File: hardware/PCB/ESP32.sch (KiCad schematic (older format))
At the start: 35 parts, among them IC5 ESP32-D0WD-V3, Q2 SS8050-G, Q3 SS8050-G, U3 ESP32_Antenna, Y1 ABS05-32.768KHZ-T, Y2 ABM11AIG-40.000MHZ-4-1Z-T

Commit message: Use added ABS05 symbol and footprint form project library
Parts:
- removed Y1: ABS05-32.768KHZ-T, ProjectFootprints:ABS05, symbol ABS05-32.768KHZ-T:ABS05-32.768KHZ-T
- added Y?: ABS05-32.768KHZ-T, ABS05, symbol ProjectLibrary:ABS05-32.768KHZ-T
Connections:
- net 32K_XN: now also Y?.2
- net 32K_XP: now also Y?.1
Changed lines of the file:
@@
 	6100 5900 6600 5900
-$Comp
-L ABS05-32.768KHZ-T:ABS05-32.768KHZ-T Y1
-U 1 1 5FE918FF
-P 1300 6750
-F 0 "Y1" H 1800 6900 50  0000 L CNN
-F 1 "ABS05-32.768KHZ-T" H 1700 6450 50  0000 C CNN
-F 2 "ProjectFootprints:ABS05" H 1950 6850 50  0001 L CNN
-F 3 "" H 1950 6750 50  0001 L CNN
-F 4 "ABRACON - ABS05-32.768KHZ-T - CRYSTAL, 32.768KHZ, 12.5PF, 1.6 X 1MM" H 1950 6650 50  0001 L CNN "Description"
-F 5 "" H 1950 6550 50  0001 L CNN "Height"
-F 6 "815-ABS05-32.768K-T" H 1950 6450 50  0001 L CNN "Mouser Part Number"
-F 7 "https://www.mouser.co.uk/ProductDetail/ABRACON/ABS05-32768KHZ-T/?qs=Pyu0ZBy%2FIJZ5hxIXB%2FLU5A%3D%3D" H 1950 6350 50  0001 L CNN "Mouser Price/Stock"
-F 8 "ABRACON" H 1950 6250 50  0001 L CNN "Manufacturer_Name"
-F 9 "ABS05-32.768KHZ-T" H 1950 6150 50  0001 L CNN "Manufacturer_Part_Number"
-	1    1300 6750
-	-1   0    0    -1
-$EndComp
 $Comp
 L Device:C C?
@@
 Wire Wire Line
 	10650 2350 10650 2500
+$Comp
+L ProjectLibrary:ABS05-32.768KHZ-T Y?
+U 1 1 5FEB4B97
+P 1300 6750
+F 0 "Y?" H 1650 7000 50  0000 L CNN
+F 1 "ABS05-32.768KHZ-T" H 1100 6900 50  0000 L CNN
+F 2 "ABS05" H 1950 6850 50  0001 L CNN
+F 3 "" H 1950 6750 50  0001 L CNN
+F 4 "ABRACON - ABS05-32.768KHZ-T - CRYSTAL, 32.768KHZ, 12.5PF, 1.6 X 1MM" H 1950 6650 50  0001 L CNN "Description"
+F 5 "815-ABS05-32.768K-T" H 1950 6450 50  0001 L CNN "Mouser Part Number"
+F 6 "https://www.mouser.co.uk/ProductDetail/ABRACON/ABS05-32768KHZ-T/?qs=Pyu0ZBy%2FIJZ5hxIXB%2FLU5A%3D%3D" H 1950 6350 50  0001 L CNN "Mouser Price/Stock"
+F 7 "ABRACON" H 1950 6250 50  0001 L CNN "Manufacturer_Name"
+F 8 "ABS05-32.768KHZ-T" H 1950 6150 50  0001 L CNN "Manufacturer_Part_Number"
+	1    1300 6750
+	-1   0    0    -1
+$EndComp
 $EndSCHEMATC

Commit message: Connect ESP32 pins
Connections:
- net SEN_RST: now reaches IC5.34 (GPIO5)
- net I2C_SCL: now reaches IC5.36 (GPIO23)
- net I2C_SDA: now reaches IC5.39 (GPIO22)
- net UART_RX: now reaches IC5.40 (U0RXD)
- net UART_TX: now reaches IC5.41 (U0TXD)
- net BAT_PWR: now reaches IC5.42 (GPIO21)
- net ESP_UART_DTR renamed UART_DTR
- net ESP_UART_RTS renamed UART_RTS
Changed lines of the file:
@@
 $EndComp
 Text HLabel 8350 2150 0    50   Input ~ 0
-ESP_UART_RTS
+UART_RTS
 Text HLabel 8350 1050 0    50   Input ~ 0
-ESP_UART_DTR
+UART_DTR
 Wire Wire Line
 	9150 1050 9250 1050
@@
 	-1   0    0    -1
 $EndComp
+Text HLabel 6600 1800 1    50   Input ~ 0
+UART_RX
+Text HLabel 6500 1800 1    50   Input ~ 0
+UART_TX
+Wire Wire Line
+	6500 1800 6500 1950
+Wire Wire Line
+	6600 1800 6600 1950
+Text HLabel 6400 1800 1    50   Input ~ 0
+BAT_PWR
+Wire Wire Line
+	6400 1950 6400 1800
+Text HLabel 7250 2850 2    50   Input ~ 0
+I2C_SCL
+Wire Wire Line
+	7250 2850 7100 2850
+Text HLabel 6700 1800 1    50   Input ~ 0
+I2C_SDA
+Wire Wire Line
+	6700 1800 6700 1950
+Text HLabel 7250 3050 2    50   Input ~ 0
+SEN_RST
+Wire Wire Line
+	7250 3050 7100 3050
 $EndSCHEMATC

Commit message: Connect Display
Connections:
- net DISP_BS: now reaches IC5.14 (GPIO25)
- net DISP_RES: now reaches IC5.15 (GPIO26)
- net DISP_SDI: now reaches IC5.17 (MTMS)
- net DISP_DC: now reaches IC5.18 (MTDI)
- net DISP_CLK: now reaches IC5.20 (MTCK)
- net DISP_CS: now reaches IC5.21 (MTDO)
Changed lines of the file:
@@
 Wire Wire Line
 	7250 3050 7100 3050
+Text HLabel 6200 5000 3    50   Input ~ 0
+DISP_CLK
+Text HLabel 6300 5000 3    50   Input ~ 0
+DISP_CS
+Text HLabel 5900 5000 3    50   Input ~ 0
+DISP_SDI
+Text HLabel 6000 5000 3    50   Input ~ 0
+DISP_DC
+Text HLabel 5150 3950 0    50   Input ~ 0
+DISP_BS
+Text HLabel 5700 5000 3    50   Input ~ 0
+DISP_RES
+Wire Wire Line
+	5300 3950 5150 3950
+Wire Wire Line
+	5700 5000 5700 4850
+Wire Wire Line
+	5900 5000 5900 4850
+Wire Wire Line
+	6000 5000 6000 4850
+Wire Wire Line
+	6200 5000 6200 4850
+Wire Wire Line
+	6300 5000 6300 4850
 $EndSCHEMATC

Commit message: correctrts, dtr connection, change spi connections, complete display connection
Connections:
- net DISP_CLK: now also IC5.17 (MTMS); no longer IC5.20 (MTCK)
- net DISP_DC: now also IC5.16 (GPIO27); no longer IC5.18 (MTDI)
- net DISP_SDI: now also IC5.20 (MTCK); no longer IC5.17 (MTMS)
- net DISP_BS1: now reaches IC5.25 (GPIO16)
- net DISP_TOUT1: now reaches IC5.27 (GPIO17)
- net DISP_BS renamed DISP_BUSY
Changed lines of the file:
@@
 Text HLabel 6600 1800 1    50   Input ~ 0
 UART_RX
-Text HLabel 6500 1800 1    50   Input ~ 0
+Text HLabel 6500 1800 1    50   Output ~ 0
 UART_TX
 Wire Wire Line
@@
 Wire Wire Line
 	6600 1800 6600 1950
-Text HLabel 6400 1800 1    50   Input ~ 0
+Text HLabel 6400 1800 1    50   Output ~ 0
 BAT_PWR
 Wire Wire Line
 	6400 1950 6400 1800
-Text HLabel 7250 2850 2    50   Input ~ 0
-I2C_SCL
-Wire Wire Line
-	7250 2850 7100 2850
 Text HLabel 6700 1800 1    50   Input ~ 0
 I2C_SDA
@@
 Wire Wire Line
 	7250 3050 7100 3050
-Text HLabel 6200 5000 3    50   Input ~ 0
+Text HLabel 5900 5000 3    50   Output ~ 0
 DISP_CLK
-Text HLabel 6300 5000 3    50   Input ~ 0
+Text HLabel 6300 5000 3    50   Output ~ 0
 DISP_CS
-Text HLabel 5900 5000 3    50   Input ~ 0
-DISP_SDI
-Text HLabel 6000 5000 3    50   Input ~ 0
+Text HLabel 5800 5000 3    50   Output ~ 0
 DISP_DC
 Text HLabel 5150 3950 0    50   Input ~ 0
-DISP_BS
-Text HLabel 5700 5000 3    50   Input ~ 0
+DISP_BUSY
+Text HLabel 5700 5000 3    50   Output ~ 0
 DISP_RES
 Wire Wire Line
@@
 Wire Wire Line
 	6300 5000 6300 4850
+Wire Wire Line
+	7250 2850 7100 2850
+Text HLabel 7250 2850 2    50   Input ~ 0
+I2C_SCL
+Text HLabel 6200 5000 3    50   Output ~ 0
+DISP_SDI
+Wire Wire Line
+	5800 4850 5800 5000
+Text HLabel 7250 3950 2    50   Output ~ 0
+DISP_BS1
+Wire Wire Line
+	7250 3950 7100 3950
+Text HLabel 7250 3750 2    50   Input ~ 0
+DISP_TOUT1
+Wire Wire Line
+	7250 3750 7100 3750
 $EndSCHEMATC

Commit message: Added debug led fixed #1
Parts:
- added LED?: APTF1616LSEEZGKQBKC, APTF1616SEEZGQBDC, symbol ProjectLibrary:APTF1616LSEEZGKQBKC
- added R?: 910, symbol Device:R
- added R? (x2): 475, symbol Device:R
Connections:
- net +3V3: now also LED?.1 (COMMON_ANODE)
- net at IC5.5 (SENSOR_VP): now also R?.1
- net at IC5.6 (SENSOR_CAPP): now also R?.1
- net at IC5.7 (SENSOR_CAPN): now also R?.1
- new net: LED?.2 (CATHODE_RED), R?.2
- new net: LED?.3 (CATHODE_GREEN), R?.2
- new net: LED?.4 (CATHODE_BLUE), R?.2
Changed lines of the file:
@@
 Wire Wire Line
 	7250 3750 7100 3750
+$Comp
+L ProjectLibrary:APTF1616LSEEZGKQBKC LED?
+U 1 1 60073962
+P 2600 5350
+F 0 "LED?" H 3600 5615 50  0000 C CNN
+F 1 "APTF1616LSEEZGKQBKC" H 3600 5524 50  0000 C CNN
+F 2 "APTF1616SEEZGQBDC" H 4450 5450 50  0001 L CNN
+F 3 "https://componentsearchengine.com/Datasheets/1/APTF1616LSEEZGKQBKC.pdf" H 4450 5350 50  0001 L CNN
+F 4 "Standard LEDs - SMD 1.6x1.6MM LOW CU RGB SMD" H 4450 5250 50  0001 L CNN "Description"
+F 5 "" H 4450 5150 50  0001 L CNN "Height"
+F 6 "604-APTF1616LSEEZGKQ" H 4450 5050 50  0001 L CNN "Mouser Part Number"
+F 7 "https://www.mouser.co.uk/ProductDetail/Kingbright/APTF1616LSEEZGKQBKC?qs=ZqXcJfGlKsh%252BpLJNPLW72w%3D%3D" H 4450 4950 50  0001 L CNN "Mouser Price/Stock"
+F 8 "Kingbright" H 4450 4850 50  0001 L CNN "Manufacturer_Name"
+F 9 "APTF1616LSEEZGKQBKC" H 4450 4750 50  0001 L CNN "Manufacturer_Part_Number"
+	1    2600 5350
+	1    0    0    -1
+$EndComp
+$Comp
+L Device:R R?
+U 1 1 60084B4A
+P 2150 4750
+F 0 "R?" H 2220 4796 50  0000 L CNN
+F 1 "910" H 2220 4705 50  0000 L CNN
+F 2 "" V 2080 4750 50  0001 C CNN
+F 3 "~" H 2150 4750 50  0001 C CNN
+	1    2150 4750
+	1    0    0    -1
+$EndComp
+$Comp
+L Device:R R?
+U 1 1 600858BD
+P 2450 4750
+F 0 "R?" H 2520 4796 50  0000 L CNN
+F 1 "475" H 2520 4705 50  0000 L CNN
+F 2 "" V 2380 4750 50  0001 C CNN
+F 3 "~" H 2450 4750 50  0001 C CNN
+	1    2450 4750
+	1    0    0    -1
+$EndComp
+$Comp
+L Device:R R?
+U 1 1 600865E9
+P 4750 4750
+F 0 "R?" H 4820 4796 50  0000 L CNN
+F 1 "475" H 4820 4705 50  0000 L CNN
+F 2 "" V 4680 4750 50  0001 C CNN
+F 3 "~" H 4750 4750 50  0001 C CNN
+	1    4750 4750
+	1    0    0    -1
+$EndComp
+$Comp
+L power:+3V3 #PWR?
+U 1 1 600A31D8
+P 4900 5250
+AR Path="/5FCFD0E2/600A31D8" Ref="#PWR?"  Part="1"
+AR Path="/5FE895CA/600A31D8" Ref="#PWR?"  Part="1"
+F 0 "#PWR?" H 4900 5100 50  0001 C CNN
+F 1 "+3V3" H 4915 5423 50  0000 C CNN
+F 2 "" H 4900 5250 50  0001 C CNN
+F 3 "" H 4900 5250 50  0001 C CNN
+	1    4900 5250
+	1    0    0    -1
+$EndComp
+Wire Wire Line
+	4600 5450 4900 5450
+Wire Wire Line
+	4900 5450 4900 5250
+Wire Wire Line
+	4600 5350 4750 5350
+Wire Wire Line
+	4750 5350 4750 4900
+Wire Wire Line
+	2600 5450 2150 5450
+Wire Wire Line
+	2150 5450 2150 4900
+Wire Wire Line
+	2600 5350 2450 5350
+Wire Wire Line
+	2450 5350 2450 4900
+Wire Wire Line
+	2450 4600 2450 4500
+Wire Wire Line
+	2450 4500 4200 4500
+Wire Wire Line
+	4200 4500 4200 3150
+Wire Wire Line
+	4200 3150 5300 3150
+Wire Wire Line
+	4300 4500 4300 3250
+Wire Wire Line
+	4300 3250 5300 3250
+Wire Wire Line
+	2150 4600 2150 4400
+Wire Wire Line
+	2150 4400 4100 4400
+Wire Wire Line
+	4100 4400 4100 3050
+Wire Wire Line
+	4100 3050 5300 3050
+Wire Wire Line
+	4750 4600 4750 4500
+Wire Wire Line
+	4300 4500 4750 4500
 $EndSCHEMATC

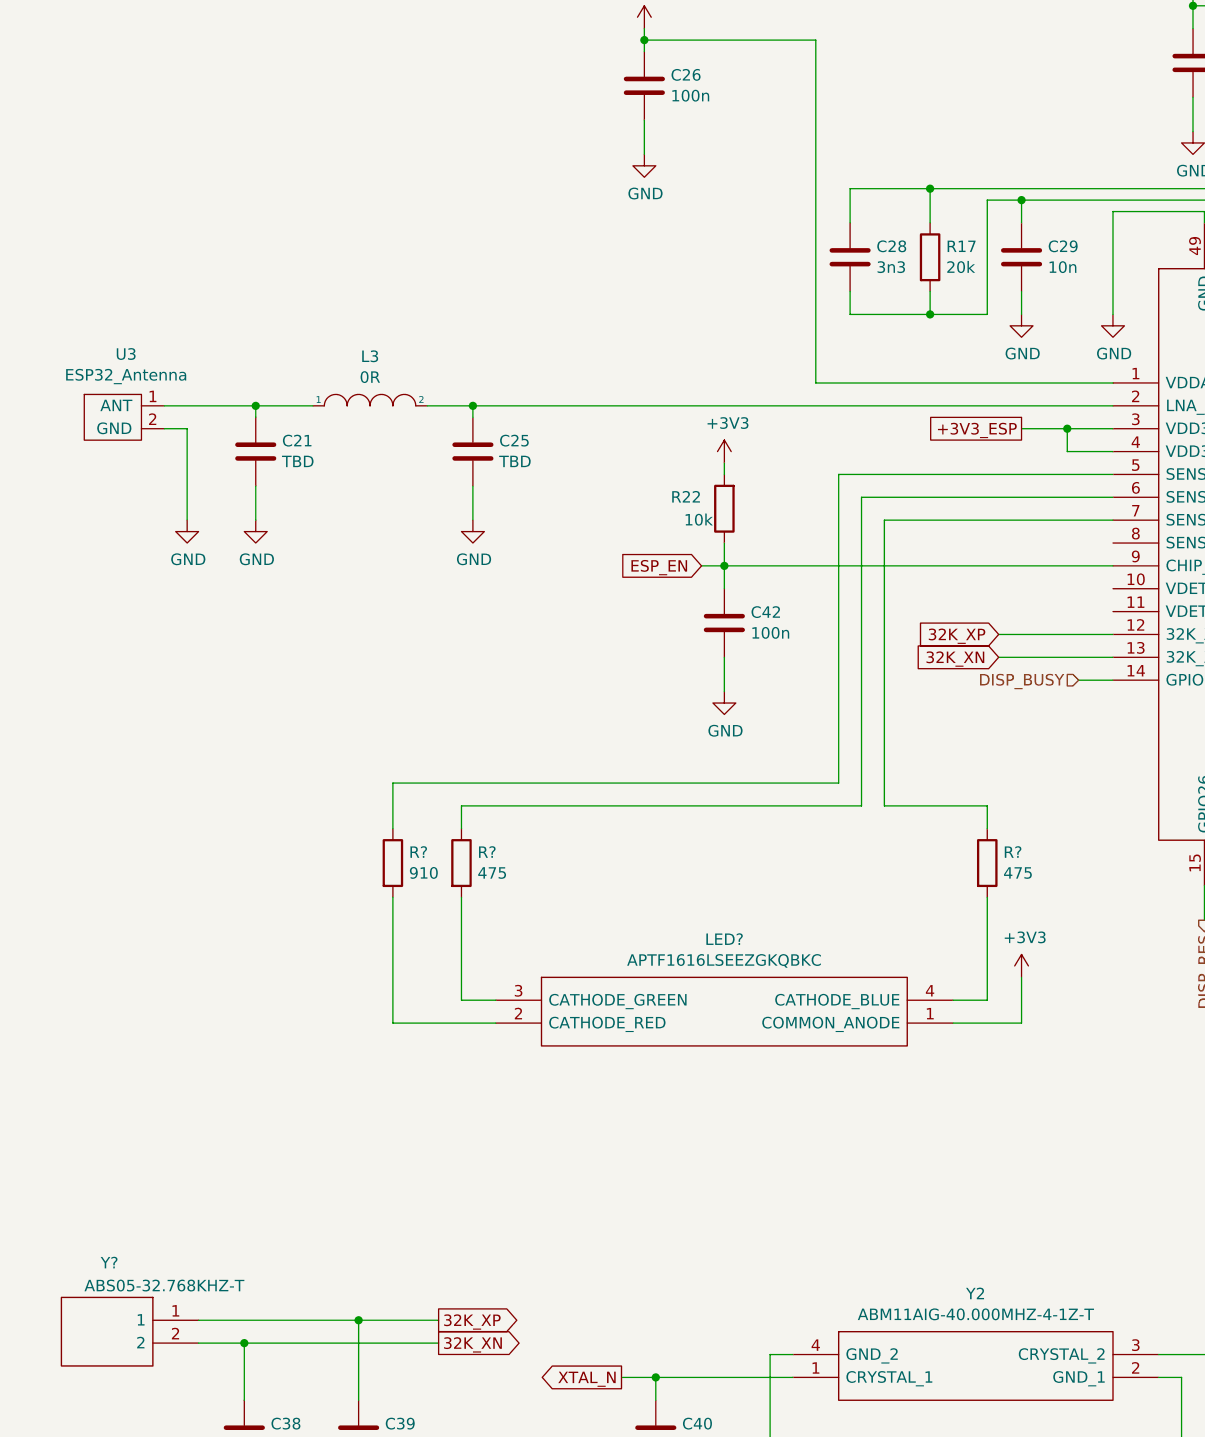
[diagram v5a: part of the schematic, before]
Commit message: add ufl connector
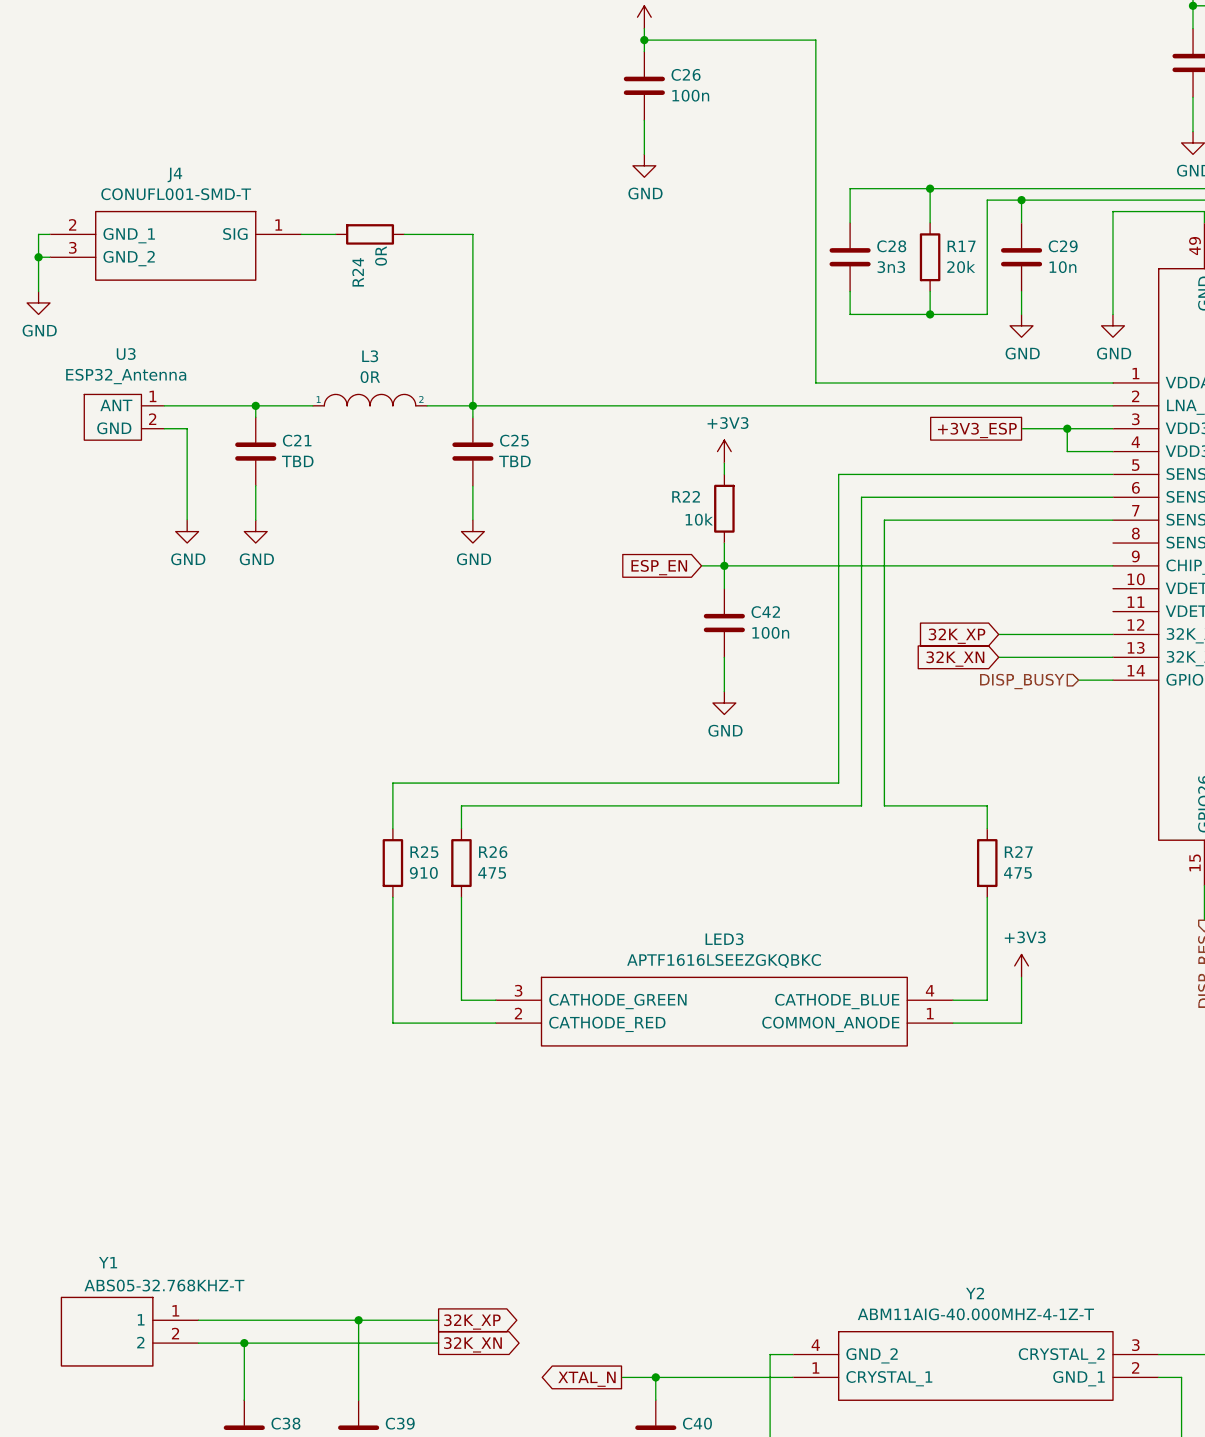
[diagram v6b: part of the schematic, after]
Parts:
- added J4: CONUFL001-SMD-T, ProjectFootprints:CONUFL001-SMD, symbol ProjectLibrary:CONUFL001-SMD-T
- added R24: 0R, Resistor_SMD:R_0603_1608Metric, symbol Device:R
- gave numbers to parts that had none: 5
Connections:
- net GND: now also J4.2 (GND_1), J4.3 (GND_2)
- net at C25.1, IC5.2 (LNA_IN), L3.2: now also R24.1
- new net: J4.1 (SIG), R24.2
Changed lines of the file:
@@
 	10650 2350 10650 2500
 $Comp
-L ProjectLibrary:ABS05-32.768KHZ-T Y?
+L ProjectLibrary:ABS05-32.768KHZ-T Y1
 U 1 1 5FEB4B97
 P 1300 6750
-F 0 "Y?" H 1650 7000 50  0000 L CNN
+F 0 "Y1" H 1650 7000 50  0000 L CNN
 F 1 "ABS05-32.768KHZ-T" H 1100 6900 50  0000 L CNN
 F 2 "ABS05" H 1950 6850 50  0001 L CNN
@@
 	7250 3750 7100 3750
 $Comp
-L ProjectLibrary:APTF1616LSEEZGKQBKC LED?
+L ProjectLibrary:APTF1616LSEEZGKQBKC LED3
 U 1 1 60073962
 P 2600 5350
-F 0 "LED?" H 3600 5615 50  0000 C CNN
+F 0 "LED3" H 3600 5615 50  0000 C CNN
 F 1 "APTF1616LSEEZGKQBKC" H 3600 5524 50  0000 C CNN
 F 2 "APTF1616SEEZGQBDC" H 4450 5450 50  0001 L CNN
@@
 $EndComp
 $Comp
-L Device:R R?
+L Device:R R25
 U 1 1 60084B4A
 P 2150 4750
-F 0 "R?" H 2220 4796 50  0000 L CNN
+F 0 "R25" H 2220 4796 50  0000 L CNN
 F 1 "910" H 2220 4705 50  0000 L CNN
 F 2 "" V 2080 4750 50  0001 C CNN
@@
 $EndComp
 $Comp
-L Device:R R?
+L Device:R R26
 U 1 1 600858BD
 P 2450 4750
-F 0 "R?" H 2520 4796 50  0000 L CNN
+F 0 "R26" H 2520 4796 50  0000 L CNN
 F 1 "475" H 2520 4705 50  0000 L CNN
 F 2 "" V 2380 4750 50  0001 C CNN
@@
 $EndComp
 $Comp
-L Device:R R?
+L Device:R R27
 U 1 1 600865E9
 P 4750 4750
-F 0 "R?" H 4820 4796 50  0000 L CNN
+F 0 "R27" H 4820 4796 50  0000 L CNN
 F 1 "475" H 4820 4705 50  0000 L CNN
 F 2 "" V 4680 4750 50  0001 C CNN
@@
 $EndComp
 $Comp
-L power:+3V3 #PWR?
+L power:+3V3 #PWR0104
 U 1 1 600A31D8
 P 4900 5250
-AR Path="/5FCFD0E2/600A31D8" Ref="#PWR?"  Part="1"
+AR Path="/5FCFD0E2/600A31D8" Ref="#PWR0104"  Part="1"
 AR Path="/5FE895CA/600A31D8" Ref="#PWR?"  Part="1"
-F 0 "#PWR?" H 4900 5100 50  0001 C CNN
+F 0 "#PWR0104" H 4900 5100 50  0001 C CNN
 F 1 "+3V3" H 4915 5423 50  0000 C CNN
 F 2 "" H 4900 5250 50  0001 C CNN
@@
 Wire Wire Line
 	4300 4500 4750 4500
+$Comp
+L Device:R R?
+U 1 1 60053A59
+P 2050 2000
+AR Path="/60053A59" Ref="R?"  Part="1"
+AR Path="/5FCFD0E2/60053A59" Ref="R24"  Part="1"
+AR Path="/5FE895CA/60053A59" Ref="R?"  Part="1"
+F 0 "R24" H 2150 1950 50  0000 L CNN
+F 1 "0R" H 2100 2050 50  0000 L CNN
+F 2 "Resistor_SMD:R_0603_1608Metric" V 1980 2000 50  0001 C CNN
+F 3 "~" H 2050 2000 50  0001 C CNN
+	1    2050 2000
+	0    1    1    0
+$EndComp
+Wire Wire Line
+	2200 2000 2500 2000
+Wire Wire Line
+	2500 2000 2500 2750
+$Comp
+L ProjectLibrary:CONUFL001-SMD-T J4
+U 1 1 6006EF78
+P 1750 2000
+F 0 "J4" H 2300 2265 50  0000 C CNN
+F 1 "CONUFL001-SMD-T" H 2300 2174 50  0000 C CNN
+F 2 "ProjectFootprints:CONUFL001-SMD" H 2700 2100 50  0001 L CNN
+F 3 "https://linxtechnologies.com/wp/product/mhf-rf-connectors/" H 2700 2000 50  0001 L CNN
+F 4 "RF Connectors / Coaxial Connectors T&R U.FL Straight Surface Mount Jack" H 2700 1900 50  0001 L CNN "Description"
+F 5 "" H 2700 1800 50  0001 L CNN "Height"
+F 6 "712-CONUFL001-SMD-T" H 2700 1700 50  0001 L CNN "Mouser Part Number"
+F 7 "https://www.mouser.co.uk/ProductDetail/Linx-Technologies/CONUFL001-SMD-T/?qs=EU6FO9ffTwfRdkBeQTdJWQ%3D%3D" H 2700 1600 50  0001 L CNN "Mouser Price/Stock"
+F 8 "Linx Technologies" H 2700 1500 50  0001 L CNN "Manufacturer_Name"
+F 9 "CONUFL001-SMD-T" H 2700 1400 50  0001 L CNN "Manufacturer_Part_Number"
+	1    1750 2000
+	-1   0    0    -1
+$EndComp
+$Comp
+L power:GND #PWR0103
+U 1 1 600794DD
+P 600 2250
+F 0 "#PWR0103" H 600 2000 50  0001 C CNN
+F 1 "GND" H 605 2077 50  0000 C CNN
+F 2 "" H 600 2250 50  0001 C CNN
+F 3 "" H 600 2250 50  0001 C CNN
+	1    600  2250
+	1    0    0    -1
+$EndComp
+Wire Wire Line
+	600  2250 600  2100
+Wire Wire Line
+	600  2000 650  2000
+Wire Wire Line
+	650  2100 600  2100
+Connection ~ 600  2100
+Wire Wire Line
+	600  2100 600  2000
+Wire Wire Line
+	1750 2000 1900 2000
 $EndSCHEMATC
